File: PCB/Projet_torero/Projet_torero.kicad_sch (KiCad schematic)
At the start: 0 parts

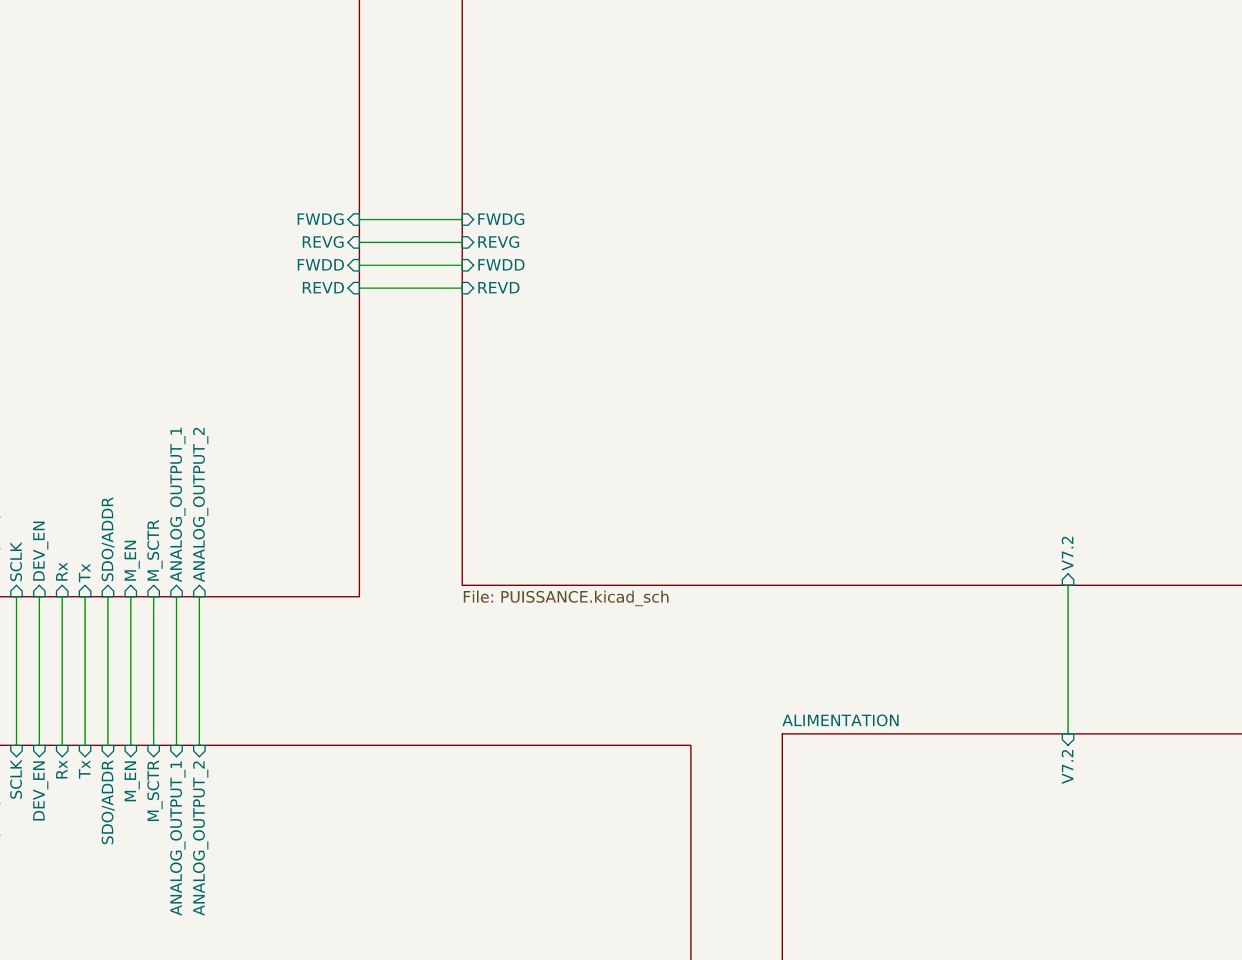
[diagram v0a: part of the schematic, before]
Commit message: modif labels hiérarchiques
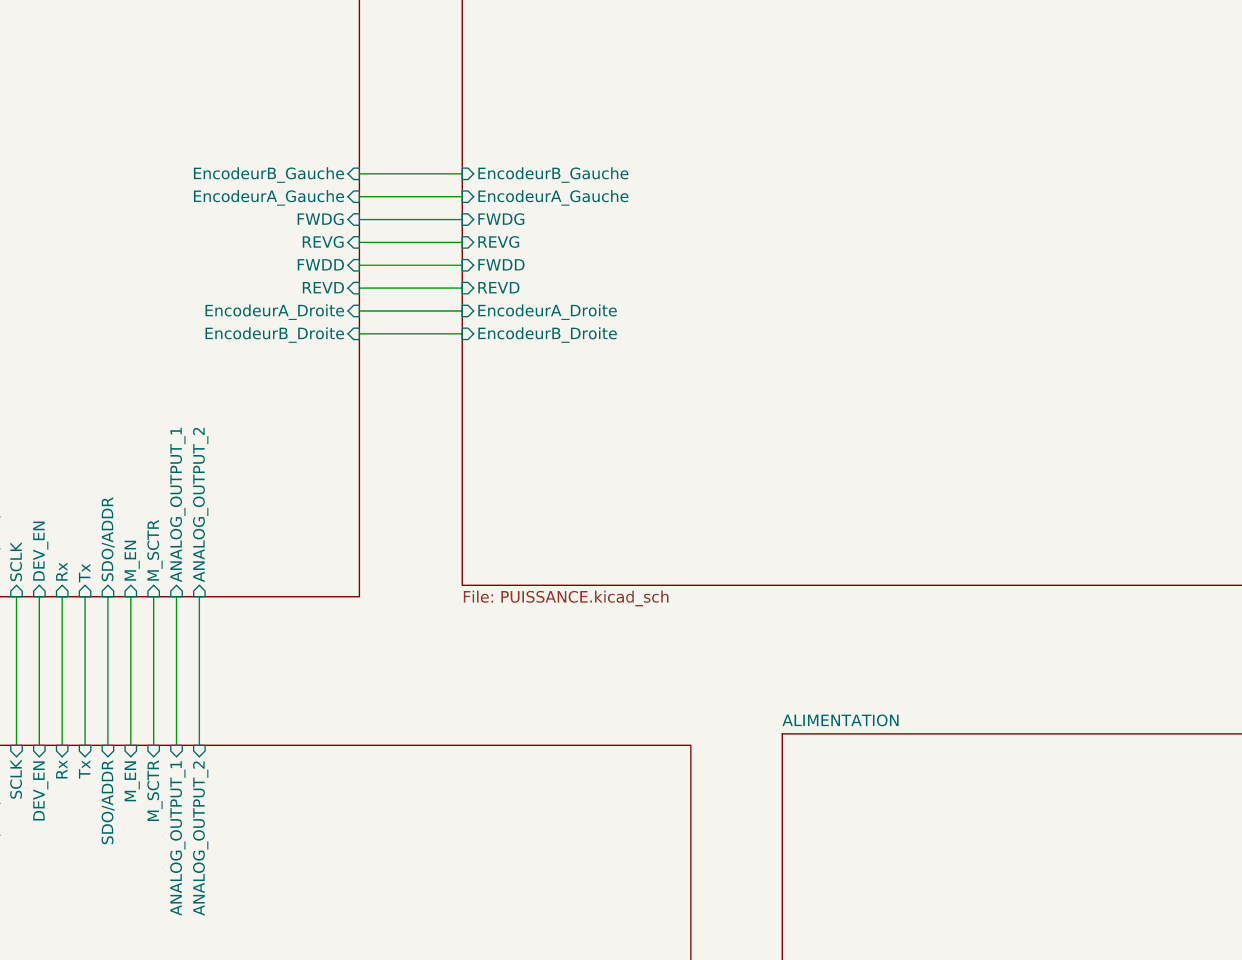
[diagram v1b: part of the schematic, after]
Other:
- sheet ALIMENTATION ports: added none; removed V7.2
- sheet PUISSANCE ports: added EncodeurA_Droite, EncodeurA_Gauche, EncodeurB_Droite, EncodeurB_Gauche; removed V7.2
- sheet STM32 ports: added EncodeurA_Droite, EncodeurA_Gauche, EncodeurB_Droite, EncodeurB_Gauche; removed none
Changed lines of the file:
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@@
+	(wire
+		(pts
+			(xy 129.54 68.58) (xy 140.97 68.58)
+		)
+		(stroke
+			(width 0)
+			(type default)
+		)
+	)
 	(wire
 		(pts
@@
 	(wire
 		(pts
+			(xy 129.54 66.04) (xy 140.97 66.04)
+		)
+		(stroke
+			(width 0)
+			(type default)
+		)
+	)
+	(wire
+		(pts
 			(xy 129.54 58.42) (xy 140.97 58.42)
 		)
@@
 	(wire
 		(pts
+			(xy 129.54 50.8) (xy 140.97 50.8)
+		)
+		(stroke
+			(width 0)
+			(type default)
+		)
+	)
+	(wire
+		(pts
 			(xy 86.36 97.79) (xy 86.36 114.3)
 		)
@@
 	(wire
 		(pts
-			(xy 208.28 96.52) (xy 208.28 113.03)
-		)
-		(stroke
-			(width 0)
-			(type default)
-		)
-	)
-	(wire
-		(pts
 			(xy 129.54 60.96) (xy 140.97 60.96)
 		)
@@
 		(pts
 			(xy 106.68 97.79) (xy 106.68 114.3)
+		)
+		(stroke
+			(width 0)
+			(type default)
+		)
+	)
+	(wire
+		(pts
+			(xy 129.54 53.34) (xy 140.97 53.34)
 		)
 		(stroke
@@
 			)
 		)
+		(pin "EncodeurB_Gauche" input
+			(at 129.54 50.8 0)
+			(effects
+				(font
+					(size 1.27 1.27)
+				)
+				(justify right)
+			)
+		)
+		(pin "EncodeurA_Gauche" input
+			(at 129.54 53.34 0)
+			(effects
+				(font
+					(size 1.27 1.27)
+				)
+				(justify right)
+			)
+		)
+		(pin "EncodeurB_Droite" input
+			(at 129.54 68.58 0)
+			(effects
+				(font
+					(size 1.27 1.27)
+				)
+				(justify right)
+			)
+		)
+		(pin "EncodeurA_Droite" input
+			(at 129.54 66.04 0)
+			(effects
+				(font
+					(size 1.27 1.27)
+				)
+				(justify right)
+			)
+		)
 		(instances
 			(project "Projet_torero"
@@
 			)
 		)
-		(pin "V7.2" input
-			(at 208.28 113.03 90)
-			(effects
-				(font
-					(size 1.27 1.27)
-				)
-				(justify right)
-			)
-		)
 		(instances
 			(project "Projet_torero"
@@
 			)
 		)
-		(pin "V7.2" input
-			(at 208.28 96.52 270)
-			(effects
-				(font
-					(size 1.27 1.27)
-				)
-				(justify left)
-			)
-		)
 		(pin "REVD" input
 			(at 140.97 63.5 180)
@@
 			(effects
 				(font
+					(size 1.27 1.27)
+				)
+				(justify left)
+			)
+		)
+		(pin "EncodeurA_Gauche" input
+			(at 140.97 53.34 180)
+			(effects
+				(font
+					(size 1.27 1.27)
+				)
+				(justify left)
+			)
+		)
+		(pin "EncodeurB_Gauche" input
+			(at 140.97 50.8 180)
+			(effects
+				(font
+					(size 1.27 1.27)
+				)
+				(justify left)
+			)
+		)
+		(pin "EncodeurA_Droite" input
+			(at 140.97 66.04 180)
+			(effects
+				(font
+					(size 1.27 1.27)
+				)
+				(justify left)
+			)
+		)
+		(pin "EncodeurB_Droite" input
+			(at 140.97 68.58 180)
+			(effects
+				(font

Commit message: ajout nouvelles feuilles capteurs bords
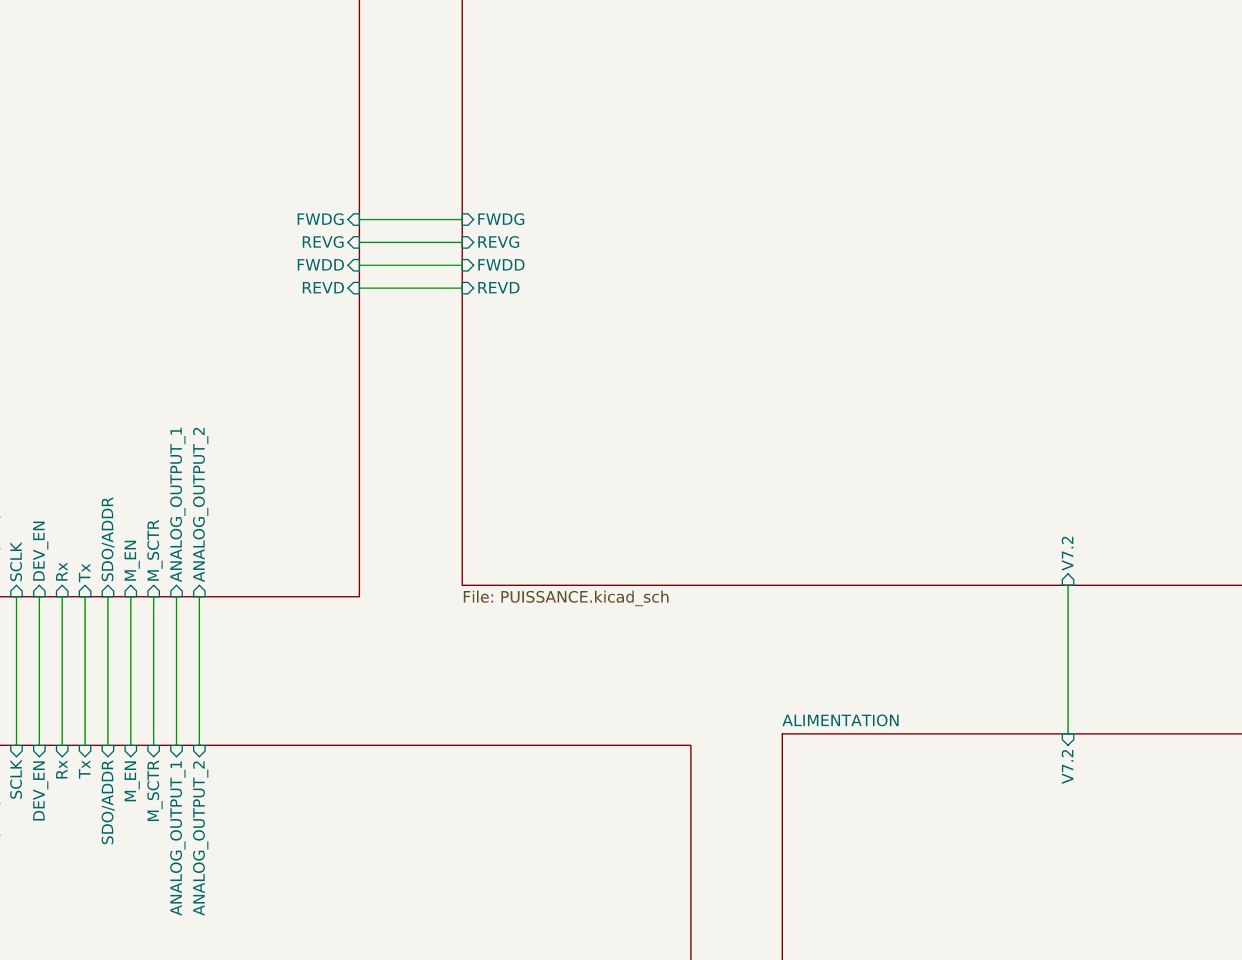
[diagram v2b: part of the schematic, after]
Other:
- sheet ALIMENTATION ports: added V7.2; removed none
- sheet PUISSANCE ports: added V7.2; removed EncodeurA_Droite, EncodeurA_Gauche, EncodeurB_Droite, EncodeurB_Gauche
- sheet STM32 ports: added none; removed EncodeurA_Droite, EncodeurA_Gauche, EncodeurB_Droite, EncodeurB_Gauche
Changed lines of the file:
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@@
-	(wire
-		(pts
-			(xy 129.54 68.58) (xy 140.97 68.58)
-		)
-		(stroke
-			(width 0)
-			(type default)
-		)
-	)
 	(wire
 		(pts
@@
 	(wire
 		(pts
-			(xy 129.54 66.04) (xy 140.97 66.04)
-		)
-		(stroke
-			(width 0)
-			(type default)
-		)
-	)
-	(wire
-		(pts
 			(xy 129.54 58.42) (xy 140.97 58.42)
 		)
@@
 	(wire
 		(pts
-			(xy 129.54 50.8) (xy 140.97 50.8)
-		)
-		(stroke
-			(width 0)
-			(type default)
-		)
-	)
-	(wire
-		(pts
 			(xy 86.36 97.79) (xy 86.36 114.3)
 		)
@@
 	(wire
 		(pts
+			(xy 208.28 96.52) (xy 208.28 113.03)
+		)
+		(stroke
+			(width 0)
+			(type default)
+		)
+	)
+	(wire
+		(pts
 			(xy 129.54 60.96) (xy 140.97 60.96)
 		)
@@
 		(pts
 			(xy 106.68 97.79) (xy 106.68 114.3)
-		)
-		(stroke
-			(width 0)
-			(type default)
-		)
-	)
-	(wire
-		(pts
-			(xy 129.54 53.34) (xy 140.97 53.34)
 		)
 		(stroke
@@
 			)
 		)
-		(pin "EncodeurB_Gauche" input
-			(at 129.54 50.8 0)
-			(effects
-				(font
-					(size 1.27 1.27)
-				)
-				(justify right)
-			)
-		)
-		(pin "EncodeurA_Gauche" input
-			(at 129.54 53.34 0)
-			(effects
-				(font
-					(size 1.27 1.27)
-				)
-				(justify right)
-			)
-		)
-		(pin "EncodeurB_Droite" input
-			(at 129.54 68.58 0)
-			(effects
-				(font
-					(size 1.27 1.27)
-				)
-				(justify right)
-			)
-		)
-		(pin "EncodeurA_Droite" input
-			(at 129.54 66.04 0)
-			(effects
-				(font
-					(size 1.27 1.27)
-				)
-				(justify right)
-			)
-		)
 		(instances
 			(project "Projet_torero"
@@
 			)
 		)
+		(pin "V7.2" input
+			(at 208.28 113.03 90)
+			(effects
+				(font
+					(size 1.27 1.27)
+				)
+				(justify right)
+			)
+		)
 		(instances
 			(project "Projet_torero"
@@
 			)
 		)
+		(pin "V7.2" input
+			(at 208.28 96.52 270)
+			(effects
+				(font
+					(size 1.27 1.27)
+				)
+				(justify left)
+			)
+		)
 		(pin "REVD" input
 			(at 140.97 63.5 180)
@@
 			(effects
 				(font
-					(size 1.27 1.27)
-				)
-				(justify left)
-			)
-		)
-		(pin "EncodeurA_Gauche" input
-			(at 140.97 53.34 180)
-			(effects
-				(font
-					(size 1.27 1.27)
-				)
-				(justify left)
-			)
-		)
-		(pin "EncodeurB_Gauche" input
-			(at 140.97 50.8 180)
-			(effects
-				(font
-					(size 1.27 1.27)
-				)
-				(justify left)
-			)
-		)
-		(pin "EncodeurA_Droite" input
-			(at 140.97 66.04 180)
-			(effects
-				(font
-					(size 1.27 1.27)
-				)
-				(justify left)
-			)
-		)
-		(pin "EncodeurB_Droite" input
-			(at 140.97 68.58 180)
-			(effects
-				(font
